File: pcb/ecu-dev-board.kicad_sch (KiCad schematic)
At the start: 0 parts

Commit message: added pickupsim section
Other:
- added sheet Pickup (Pickup.kicad_sch)
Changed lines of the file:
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@@
 	(generator_version "9.0")
 	(paper "A4")
+	(sheet
+		(at 38.1 25.4)
+		(size 93.98 62.23)
+		(exclude_from_sim no)
+		(in_bom yes)
+		(on_board yes)
+		(dnp no)
+		(fields_autoplaced yes)
+		(stroke
+			(width 0.1524)
+			(type solid)
+		)
+		(fill
+			(color 0 0 0 0.0000)
+		)
+		(property "Sheetname" "Pickup"
+			(at 38.1 24.6884 0)
+			(effects
+				(font
+					(size 1.27 1.27)
+				)
+				(justify left bottom)
+			)
+		)
+		(property "Sheetfile" "Pickup.kicad_sch"
+			(at 38.1 88.2146 0)
+			(effects
+				(font
+					(size 1.27 1.27)
+				)
+				(justify left top)
+			)
+		)
+		(instances
+			(project "ecu-dev-board"
+				(path "/38d4df77-b5a0-4642-8410-8b13c21c2c3b"
+					(page "2")
+				)
+			)
+		)
+	)
 	(sheet_instances
 		(path "/"

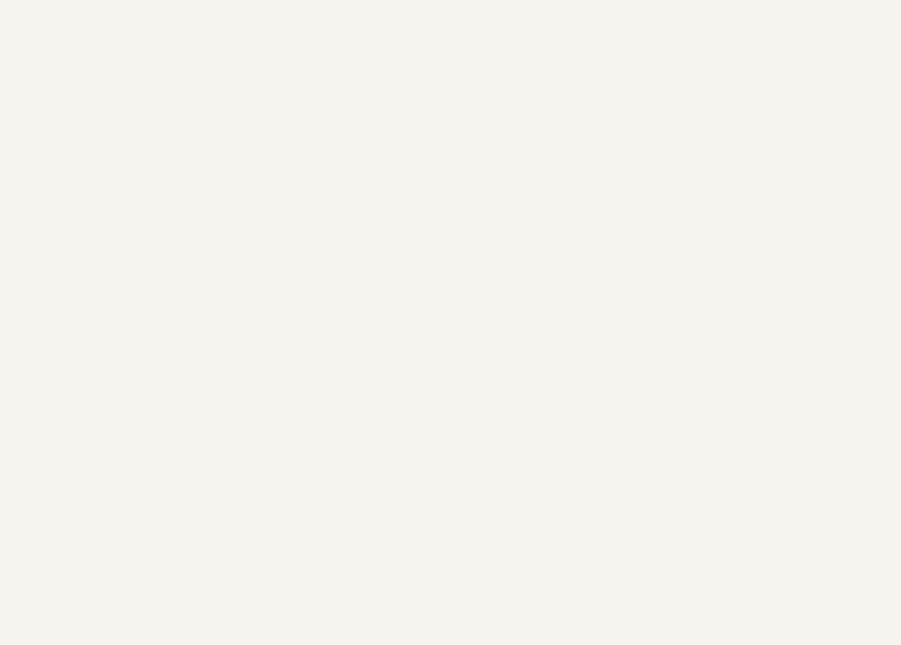
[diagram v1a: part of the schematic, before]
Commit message: created MCU sheet
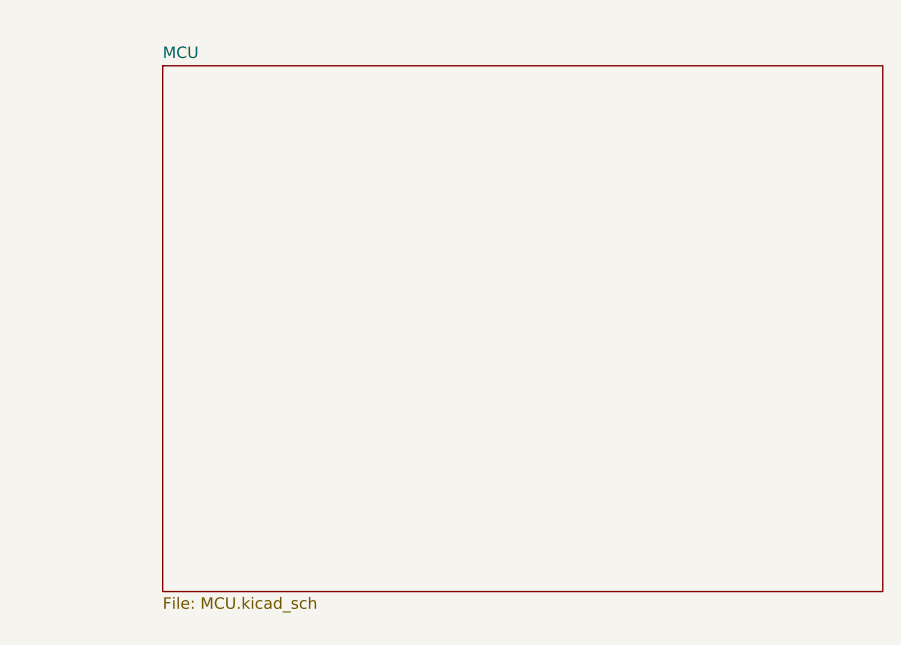
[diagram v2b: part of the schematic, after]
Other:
- added sheet MCU (MCU.kicad_sch)
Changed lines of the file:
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@@
+		)
+	)
+	(sheet
+		(at 177.8 27.94)
+		(size 80.01 58.42)
+		(exclude_from_sim no)
+		(in_bom yes)
+		(on_board yes)
+		(dnp no)
+		(fields_autoplaced yes)
+		(stroke
+			(width 0.1524)
+			(type solid)
+		)
+		(fill
+			(color 0 0 0 0.0000)
+		)
+		(property "Sheetname" "MCU"
+			(at 177.8 27.2284 0)
+			(effects
+				(font
+					(size 1.27 1.27)
+				)
+				(justify left bottom)
+			)
+		)
+		(property "Sheetfile" "MCU.kicad_sch"
+			(at 177.8 86.9446 0)
+			(effects
+				(font
+					(size 1.27 1.27)
+				)
+				(justify left top)
+			)
+		)
+		(instances
+			(project "ecu-dev-board"
+				(path "/38d4df77-b5a0-4642-8410-8b13c21c2c3b"
+					(page "3")
+				)
+			)
 		)
 	)

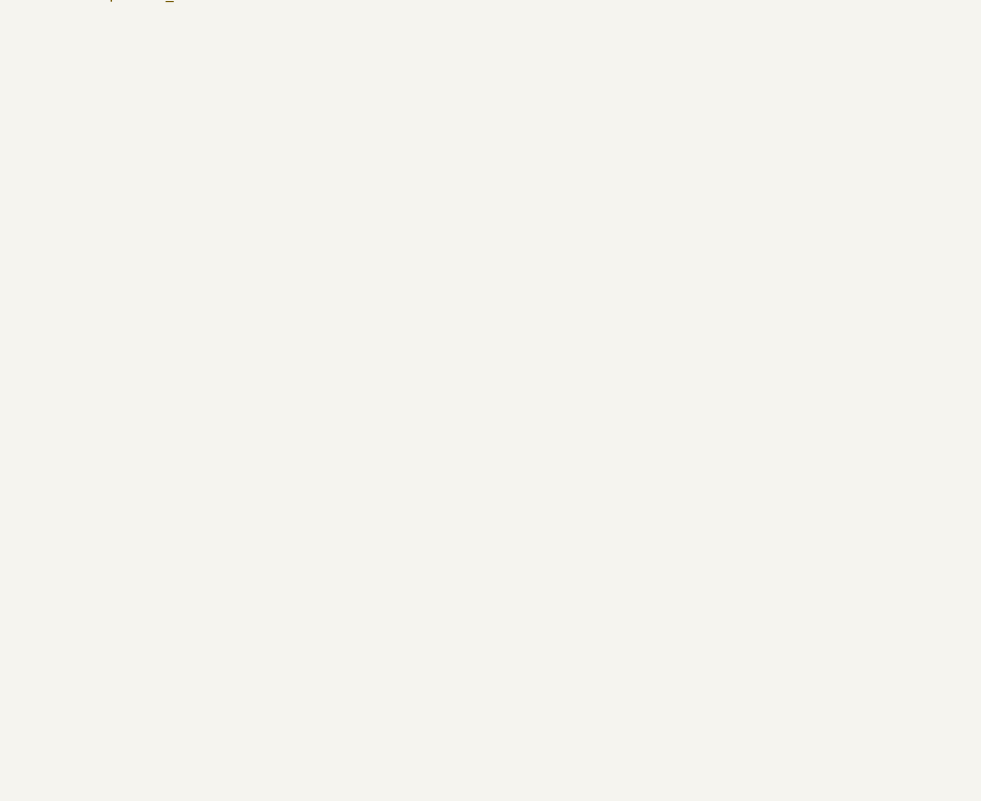
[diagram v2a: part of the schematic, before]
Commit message: added SSR
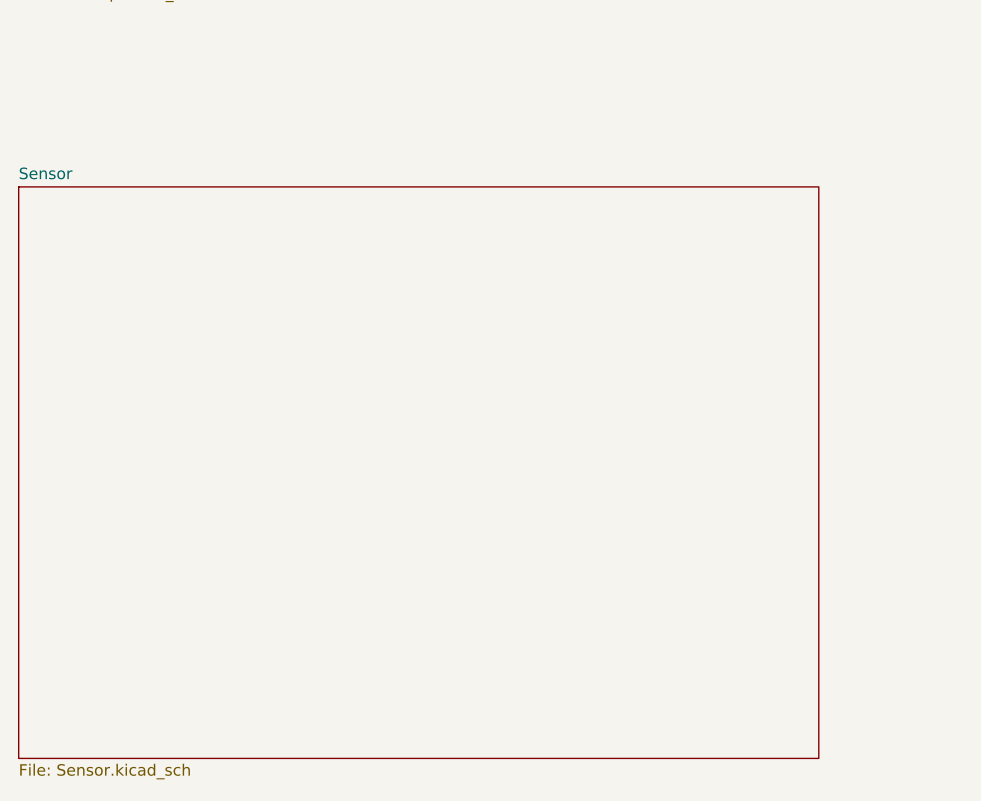
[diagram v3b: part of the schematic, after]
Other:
- added sheet Sensor (Sensor.kicad_sch)
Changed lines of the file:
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@@
+	)
+	(sheet
+		(at 36.83 110.49)
+		(size 88.9 63.5)
+		(exclude_from_sim no)
+		(in_bom yes)
+		(on_board yes)
+		(dnp no)
+		(fields_autoplaced yes)
+		(stroke
+			(width 0.1524)
+			(type solid)
+		)
+		(fill
+			(color 0 0 0 0.0000)
+		)
+		(property "Sheetname" "Sensor"
+			(at 36.83 109.7784 0)
+			(effects
+				(font
+					(size 1.27 1.27)
+				)
+				(justify left bottom)
+			)
+		)
+		(property "Sheetfile" "Sensor.kicad_sch"
+			(at 36.83 174.5746 0)
+			(effects
+				(font
+					(size 1.27 1.27)
+				)
+				(justify left top)
+			)
+		)
+		(instances
+			(project "ecu-dev-board"
+				(path "/38d4df77-b5a0-4642-8410-8b13c21c2c3b"
+					(page "4")
+				)
+			)
+		)
 	)
 	(sheet

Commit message: added CDI
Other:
- added sheet CDI (CDI.kicad_sch)
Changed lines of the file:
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@@
+		)
+	)
+	(sheet
+		(at 179.07 106.68)
+		(size 77.47 50.8)
+		(exclude_from_sim no)
+		(in_bom yes)
+		(on_board yes)
+		(dnp no)
+		(fields_autoplaced yes)
+		(stroke
+			(width 0.1524)
+			(type solid)
+		)
+		(fill
+			(color 0 0 0 0.0000)
+		)
+		(property "Sheetname" "CDI"
+			(at 179.07 105.9684 0)
+			(effects
+				(font
+					(size 1.27 1.27)
+				)
+				(justify left bottom)
+			)
+		)
+		(property "Sheetfile" "CDI.kicad_sch"
+			(at 179.07 158.0646 0)
+			(effects
+				(font
+					(size 1.27 1.27)
+				)
+				(justify left top)
+			)
+		)
+		(instances
+			(project "ecu-dev-board"
+				(path "/38d4df77-b5a0-4642-8410-8b13c21c2c3b"
+					(page "5")
+				)
+			)
 		)
 	)

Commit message: small fix
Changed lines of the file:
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@@
 	)
 	(sheet
-		(at 36.83 110.49)
+		(at 38.1 107.95)
 		(size 88.9 63.5)
 		(exclude_from_sim no)
@@
 		)
 		(property "Sheetname" "Sensor"
-			(at 36.83 109.7784 0)
+			(at 38.1 107.2384 0)
 			(effects
 				(font
@@
 		)
 		(property "Sheetfile" "Sensor.kicad_sch"
-			(at 36.83 174.5746 0)
+			(at 38.1 172.0346 0)
 			(effects
 				(font

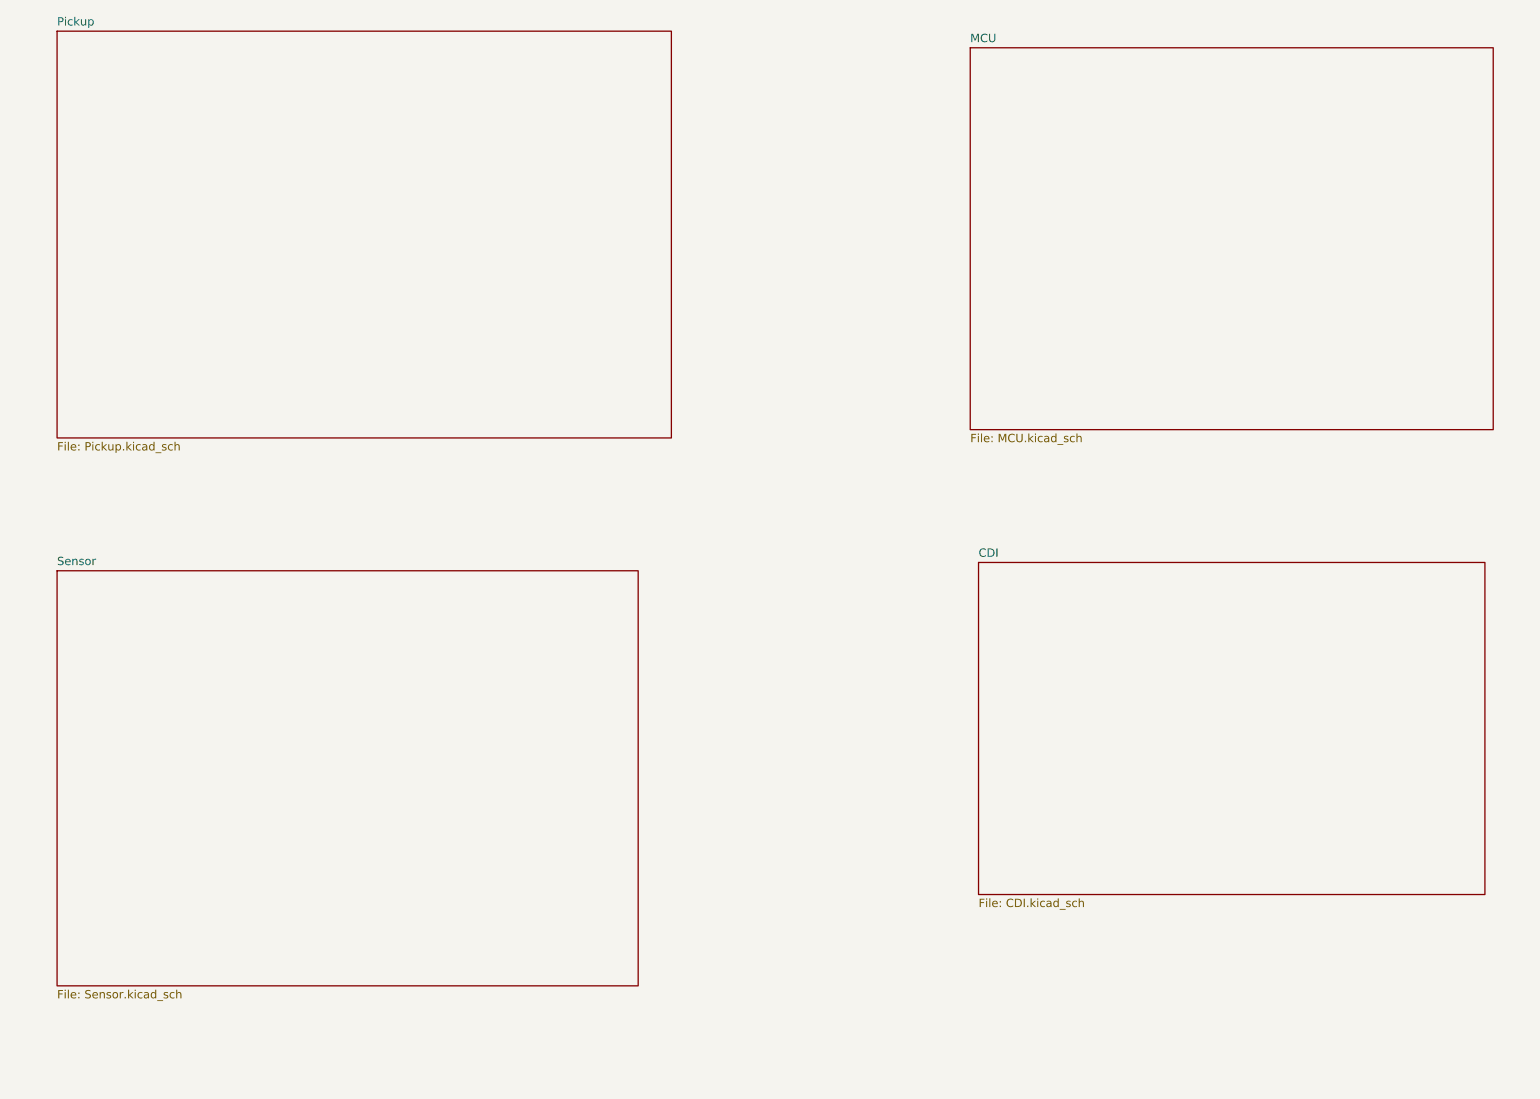
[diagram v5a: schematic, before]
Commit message: added batteryless function
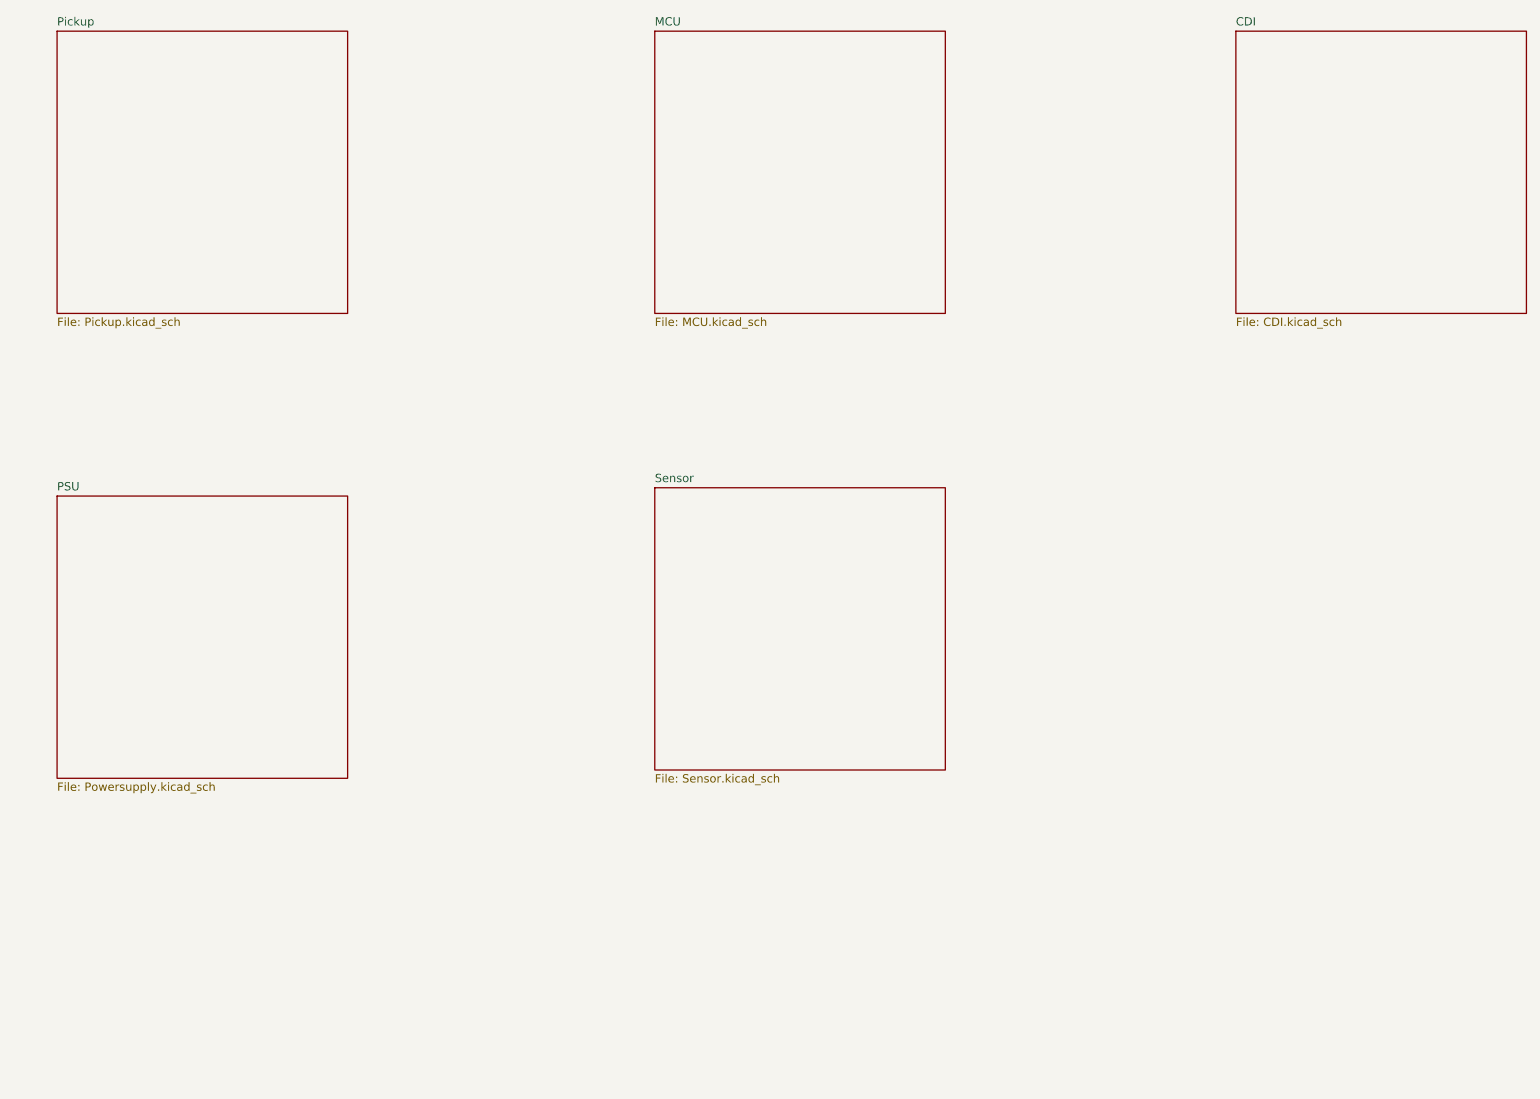
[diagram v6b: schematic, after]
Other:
- added sheet PSU (Powersupply.kicad_sch)
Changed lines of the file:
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@@
 	(sheet
 		(at 38.1 25.4)
-		(size 93.98 62.23)
+		(size 44.45 43.18)
 		(exclude_from_sim no)
 		(in_bom yes)
@@
 		)
 		(property "Sheetfile" "Pickup.kicad_sch"
-			(at 38.1 88.2146 0)
+			(at 38.1 69.1646 0)
 			(effects
 				(font
@@
 	)
 	(sheet
-		(at 38.1 107.95)
-		(size 88.9 63.5)
+		(at 129.54 95.25)
+		(size 44.45 43.18)
 		(exclude_from_sim no)
 		(in_bom yes)
@@
 		)
 		(property "Sheetname" "Sensor"
-			(at 38.1 107.2384 0)
+			(at 129.54 94.5384 0)
 			(effects
 				(font
@@
 		)
 		(property "Sheetfile" "Sensor.kicad_sch"
-			(at 38.1 172.0346 0)
+			(at 129.54 139.0146 0)
 			(effects
 				(font
@@
 	)
 	(sheet
-		(at 177.8 27.94)
-		(size 80.01 58.42)
+		(at 38.1 96.52)
+		(size 44.45 43.18)
+		(exclude_from_sim no)
+		(in_bom yes)
+		(on_board yes)
+		(dnp no)
+		(fields_autoplaced yes)
+		(stroke
+			(width 0.1524)
+			(type solid)
+		)
+		(fill
+			(color 0 0 0 0.0000)
+		)
+		(property "Sheetname" "PSU"
+			(at 38.1 95.8084 0)
+			(effects
+				(font
+					(size 1.27 1.27)
+				)
+				(justify left bottom)
+			)
+		)
+		(property "Sheetfile" "Powersupply.kicad_sch"
+			(at 38.1 140.2846 0)
+			(effects
+				(font
+					(size 1.27 1.27)
+				)
+				(justify left top)
+			)
+		)
+		(instances
+			(project "ecu-dev-board"
+				(path "/38d4df77-b5a0-4642-8410-8b13c21c2c3b"
+					(page "6")
+				)
+			)
+		)
+	)
+	(sheet
+		(at 129.54 25.4)
+		(size 44.45 43.18)
 		(exclude_from_sim no)
 		(in_bom yes)
@@
 		)
 		(property "Sheetname" "MCU"
-			(at 177.8 27.2284 0)
+			(at 129.54 24.6884 0)
 			(effects
 				(font
@@
 		)
 		(property "Sheetfile" "MCU.kicad_sch"
-			(at 177.8 86.9446 0)
+			(at 129.54 69.1646 0)
 			(effects
 				(font
@@
 	)
 	(sheet
-		(at 179.07 106.68)
-		(size 77.47 50.8)
+		(at 218.44 25.4)
+		(size 44.45 43.18)
 		(exclude_from_sim no)
 		(in_bom yes)
@@
 		)
 		(property "Sheetname" "CDI"
-			(at 179.07 105.9684 0)
+			(at 218.44 24.6884 0)
 			(effects
 				(font
@@
 		)
 		(property "Sheetfile" "CDI.kicad_sch"
-			(at 179.07 158.0646 0)
+			(at 218.44 69.1646 0)
 			(effects
 				(font
